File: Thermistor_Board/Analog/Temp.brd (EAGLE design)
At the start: 70 x 70 mm, 39 parts, among them J1 IO, J2 SJ-3523-SMT-TR, J3 SJ-3523-SMT-TR, J5 SJ-3523-SMT-TR

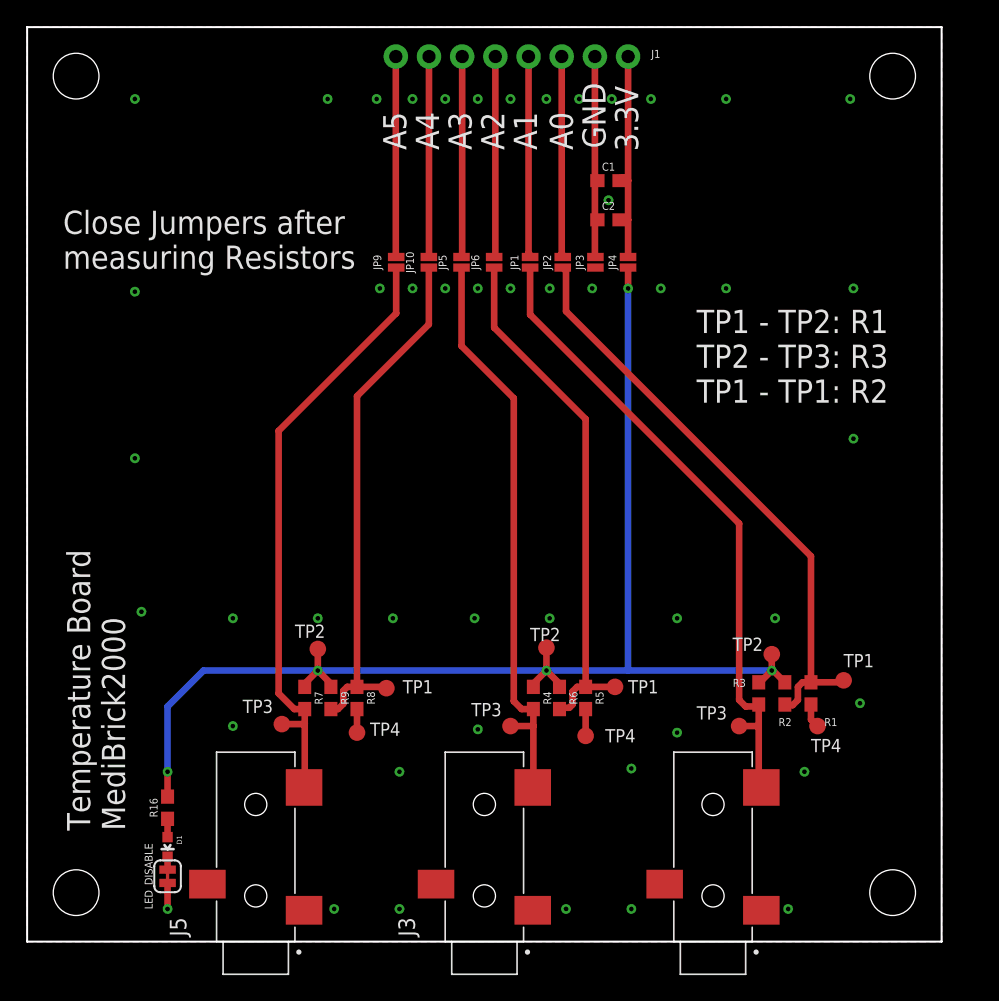
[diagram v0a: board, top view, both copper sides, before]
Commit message: Board Updates
All LEDs at same location
Separated analog and digital ground
Updated impedance components
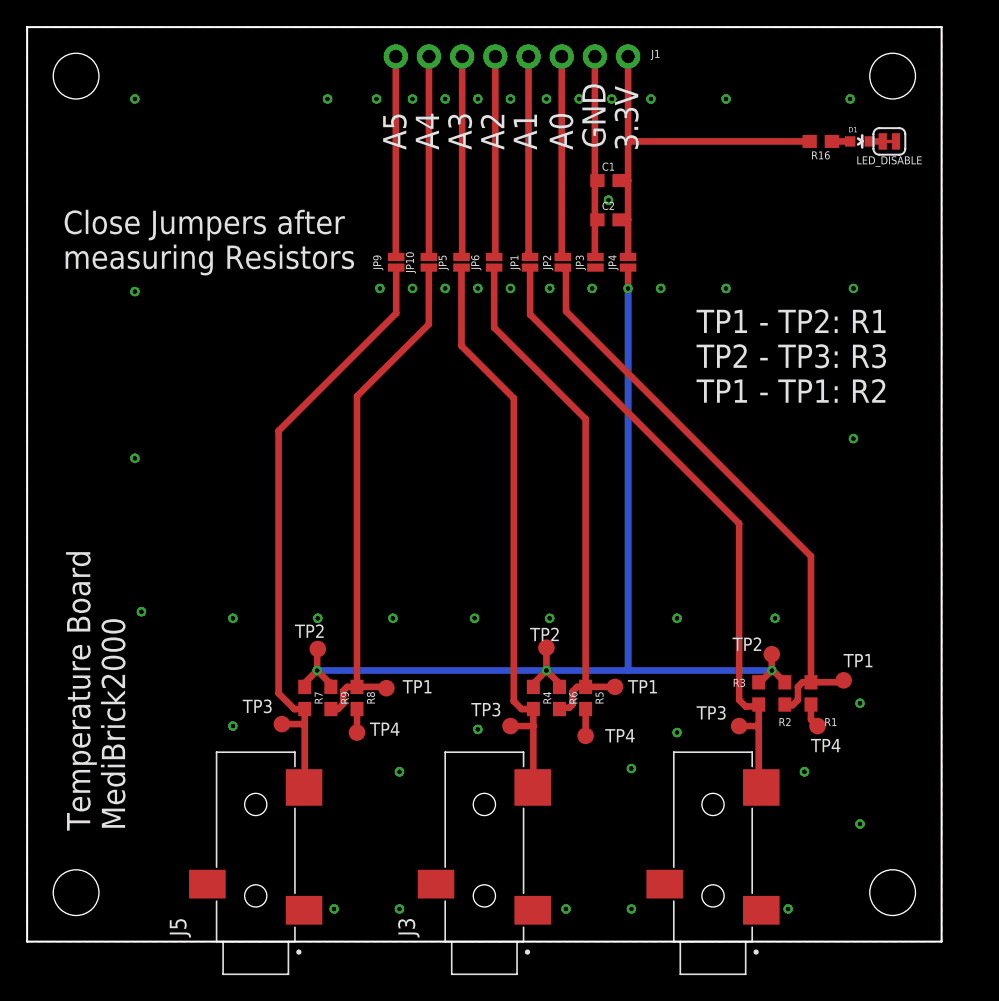
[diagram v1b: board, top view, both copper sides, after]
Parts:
- moved LED_DISABLE 78.8 mm to (66.0, 61.2), turned to 180 degrees
- moved D1 75.7 mm to (63.8, 61.2), turned to 270 degrees
- moved R16 71.4 mm to (60.8, 61.2), turned to 180 degrees
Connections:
- removed net N$12: J1.5, JP6.2
- net 3.3V: no longer R16.2
- net N$15: now also R16.2
- net N$16: now also J1.5, JP6.2
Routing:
- net 3.3V: track 99.7 -> 80.3 mm, vias 5 -> 4
- net N$16: track 16.0 -> 31.3 mm
- net N$12: track 15.4 -> 0.00 mm
- net N$15: track 17.2 -> 31.1 mm
- net GND: track 7.70 -> 5.71 mm
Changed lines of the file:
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@@
 <attribute name="VALUE" x="44.5" y="54.488" size="0.6096" layer="27" font="vector" ratio="20" align="top-center"/>
 </element>
-<element name="R16" library="SparkFun-Resistors" library_urn="urn:adsk.eagle:library:532" package="0603" package3d_urn="urn:adsk.eagle:package:39650/1" value="1k" x="10.75" y="10.25" smashed="yes" rot="R90">
-<attribute name="NAME" x="9.988" y="10.25" size="0.6096" layer="25" font="vector" ratio="20" rot="R90" align="bottom-center"/>
-<attribute name="PROD_ID" value="RES-07856" x="10.75" y="10.25" size="1.778" layer="27" rot="R90" display="off"/>
-<attribute name="VALUE" x="11.512" y="10.25" size="0.6096" layer="27" font="vector" ratio="20" rot="R90" align="top-center"/>
-</element>
-<element name="D1" library="SparkFun-LED" package="LED-0603" value="RED" x="10.75" y="7.25" smashed="yes" rot="R180">
-<attribute name="NAME" x="11.4485" y="8.139" size="0.4064" layer="25" rot="R270"/>
-<attribute name="PROD_ID" value="DIO-00819" x="13.75" y="0.25" size="1.778" layer="27" rot="R180" display="off"/>
-<attribute name="VALUE" x="9.6705" y="8.266" size="0.4064" layer="27" rot="R270"/>
-</element>
-<element name="LED_DISABLE" library="SparkFun-Jumpers" library_urn="urn:adsk.eagle:library:528" package="SMT-JUMPER_2_NC_TRACE_SILK" package3d_urn="urn:adsk.eagle:package:39281/1" value="JUMPER-SMT_2_NC_TRACE_SILK" x="10.75" y="5" smashed="yes" rot="R90">
-<attribute name="NAME" x="9.607" y="5" size="0.6096" layer="25" font="vector" ratio="20" rot="R90" align="bottom-center"/>
-<attribute name="VALUE" x="11.893" y="5" size="0.6096" layer="27" font="vector" ratio="20" rot="R90" align="top-center"/>
+<element name="R16" library="SparkFun-Resistors" library_urn="urn:adsk.eagle:library:532" package="0603" package3d_urn="urn:adsk.eagle:package:39650/1" value="1k" x="60.75" y="61.25" smashed="yes" rot="R180">
+<attribute name="NAME" x="60.75" y="60.488" size="0.6096" layer="25" font="vector" ratio="20" rot="R180" align="bottom-center"/>
+<attribute name="PROD_ID" value="RES-07856" x="60.75" y="61.25" size="1.778" layer="27" rot="R180" display="off"/>
+<attribute name="VALUE" x="60.75" y="62.012" size="0.6096" layer="27" font="vector" ratio="20" rot="R180" align="top-center"/>
+</element>
+<element name="D1" library="SparkFun-LED" package="LED-0603" value="RED" x="63.75" y="61.25" smashed="yes" rot="R270">
+<attribute name="NAME" x="62.861" y="61.9485" size="0.4064" layer="25"/>
+<attribute name="PROD_ID" value="DIO-00819" x="70.75" y="64.25" size="1.778" layer="27" rot="R270" display="off"/>
+<attribute name="VALUE" x="62.734" y="60.1705" size="0.4064" layer="27"/>
+</element>
+<element name="LED_DISABLE" library="SparkFun-Jumpers" library_urn="urn:adsk.eagle:library:528" package="SMT-JUMPER_2_NC_TRACE_SILK" package3d_urn="urn:adsk.eagle:package:39281/1" value="JUMPER-SMT_2_NC_TRACE_SILK" x="66" y="61.25" smashed="yes" rot="R180">
+<attribute name="NAME" x="66" y="60.107" size="0.6096" layer="25" font="vector" ratio="20" rot="R180" align="bottom-center"/>
+<attribute name="VALUE" x="66" y="62.393" size="0.6096" layer="27" font="vector" ratio="20" rot="R180" align="top-center"/>
 </element>
 <element name="FRAME1" library="SparkFun-Aesthetics" library_urn="urn:adsk.eagle:library:507" package="DUMMY" package3d_urn="urn:adsk.eagle:package:37104/1" value="FRAME-LETTERNO_PACKAGE" x="-0.25" y="-5.25" smashed="yes">
@@
 <signals>
 <signal name="3.3V">
-<contactref element="R16" pad="2"/>
-<via x="10.75" y="13" extent="1-16" drill="0.35"/>
-<wire x1="10.75" y1="11.1" x2="10.75" y2="13" width="0.508" layer="1"/>
 <via x="57" y="20.75" extent="1-16" drill="0.35"/>
-<wire x1="13.5" y1="20.75" x2="10.75" y2="18" width="0.508" layer="16"/>
-<wire x1="10.75" y1="18" x2="10.75" y2="13" width="0.508" layer="16"/>
 <wire x1="57" y1="20.75" x2="46" y2="20.75" width="0.508" layer="16"/>
 <wire x1="46" y1="20.75" x2="39.75" y2="20.75" width="0.508" layer="16"/>
@@
 <contactref element="JP4" pad="1"/>
 <contactref element="TP1" pad="P$1"/>
-<wire x1="39.75" y1="20.75" x2="22.25" y2="20.75" width="0.508" layer="16"/>
-<wire x1="22.25" y1="20.75" x2="13.5" y2="20.75" width="0.508" layer="16"/>
+<wire x1="39.75" y1="20.75" x2="22.2" y2="20.75" width="0.508" layer="16"/>
 <wire x1="57" y1="22" x2="57" y2="21.5" width="0.508" layer="1"/>
 <contactref element="R9" pad="1"/>
@@
 <wire x1="57" y1="20.75" x2="57.1" y2="20.75" width="0.508" layer="1"/>
 <wire x1="57.1" y1="20.75" x2="58" y2="19.85" width="0.508" layer="1"/>
-<via x="22.25" y="20.75" extent="1-16" drill="0.35"/>
-<wire x1="21.25" y1="19.5" x2="21.25" y2="19.75" width="0.508" layer="1"/>
-<wire x1="21.25" y1="19.75" x2="22.25" y2="20.75" width="0.508" layer="1"/>
-<wire x1="22.25" y1="20.75" x2="23.25" y2="19.75" width="0.508" layer="1"/>
-<wire x1="23.25" y1="19.75" x2="23.25" y2="19.5" width="0.508" layer="1"/>
-<wire x1="22.25" y1="20.75" x2="22.25" y2="22.4" width="0.508" layer="1"/>
+<via x="22.2" y="20.75" extent="1-16" drill="0.35"/>
+<wire x1="21.25" y1="19.5" x2="21.25" y2="19.8" width="0.508" layer="1"/>
+<wire x1="21.25" y1="19.8" x2="22.2" y2="20.75" width="0.508" layer="1"/>
+<wire x1="23.25" y1="19.809809375" x2="23.146109375" y2="19.803890625" width="0.508" layer="1"/>
+<wire x1="22.2" y1="20.75" x2="23.146109375" y2="19.803890625" width="0.508" layer="1"/>
+<wire x1="23.25" y1="19.809809375" x2="23.25" y2="19.5" width="0.508" layer="1"/>
+<wire x1="22.25" y1="22.4" x2="22.2" y2="22.35" width="0.508" layer="1"/>
+<wire x1="22.2" y1="22.35" x2="22.2" y2="20.75" width="0.508" layer="1"/>
 <via x="46" y="50" extent="1-16" drill="0.35"/>
 <wire x1="46" y1="50" x2="46" y2="20.75" width="0.508" layer="16"/>
@@
 <via x="8.25" y="64.5" extent="1-16" drill="0.35"/>
 <contactref element="LED_DISABLE" pad="1"/>
-<wire x1="10.75" y1="4.492" x2="10.75" y2="2.5" width="0.508" layer="1"/>
-<via x="10.75" y="2.5" extent="1-16" drill="0.35"/>
+<via x="63.75" y="9" extent="1-16" drill="0.35"/>
 <polygon width="0.508" layer="16" isolate="0.254">
 <vertex x="0" y="70"/>
@@
 <contactref element="R16" pad="1"/>
 <contactref element="D1" pad="A"/>
-<wire x1="10.75" y1="9.4" x2="10.75" y2="8" width="0.508" layer="1"/>
+<wire x1="61.6" y1="61.25" x2="63" y2="61.25" width="0.508" layer="1"/>
 </signal>
 <signal name="N$28">
 <contactref element="D1" pad="C"/>
 <contactref element="LED_DISABLE" pad="2"/>
-<wire x1="10.75" y1="5.508" x2="10.75" y2="6.5" width="0.508" layer="1"/>
+<wire x1="65.492" y1="61.25" x2="64.5" y2="61.25" width="0.508" layer="1"/>
 </signal>
 <signal name="N$1">
@@
 <wire x1="30.76" y1="52.4164" x2="30.75" y2="52.4064" width="0.508" layer="1"/>
 </signal>
-<signal name="N$12">
-<contactref element="J1" pad="5"/>
-<contactref element="JP6" pad="2"/>
-<wire x1="35.84" y1="67.75" x2="35.84" y2="52.4964" width="0.508" layer="1"/>
-<wire x1="35.84" y1="52.4964" x2="35.75" y2="52.4064" width="0.508" layer="1"/>
-</signal>
 <signal name="N$10">
 <contactref element="JP9" pad="2"/>
@@
 <wire x1="45.875" y1="58.375" x2="45.75" y2="58.5" width="0.508" layer="1"/>
 <wire x1="45.75" y1="58.5" x2="45.5" y2="58.5" width="0.508" layer="1"/>
-<wire x1="46" y1="67.75" x2="46" y2="58.25" width="0.508" layer="1"/>
+<wire x1="46" y1="67.75" x2="46" y2="61.25" width="0.508" layer="1"/>
+<wire x1="46" y1="61.25" x2="46" y2="58.25" width="0.508" layer="1"/>
 <wire x1="45.35" y1="58.25" x2="45.475" y2="58.375" width="0.508" layer="1"/>
 <wire x1="45.475" y1="58.375" x2="45.875" y2="58.375" width="0.508" layer="1"/>
+<contactref element="R16" pad="2"/>
+<wire x1="59.9" y1="61.25" x2="46" y2="61.25" width="0.508" layer="1"/>
 </signal>
 <signal name="N$16">
@@
 <wire x1="43.5" y1="52.4064" x2="43.46" y2="52.4464" width="0.508" layer="1"/>
 <wire x1="43.46" y1="52.4464" x2="43.46" y2="52.6115" width="0.508" layer="1"/>
+<contactref element="J1" pad="5"/>
+<contactref element="JP6" pad="2"/>
+<wire x1="35.84" y1="67.75" x2="35.84" y2="52.4964" width="0.508" layer="1"/>
+<wire x1="35.84" y1="52.4964" x2="35.75" y2="52.4064" width="0.508" layer="1"/>
+<wire x1="35.84" y1="67.75" x2="43.46" y2="67.75" width="0" layer="19" extent="1-1"/>
 </signal>
 </signals>

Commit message: Board Updates
Separated analog and digital ground
Updated routing
Updated silk labeling
Sound board with ES8388 included
Impedance and ECG board
Working on IMU board
Working on Environmental Airquality board
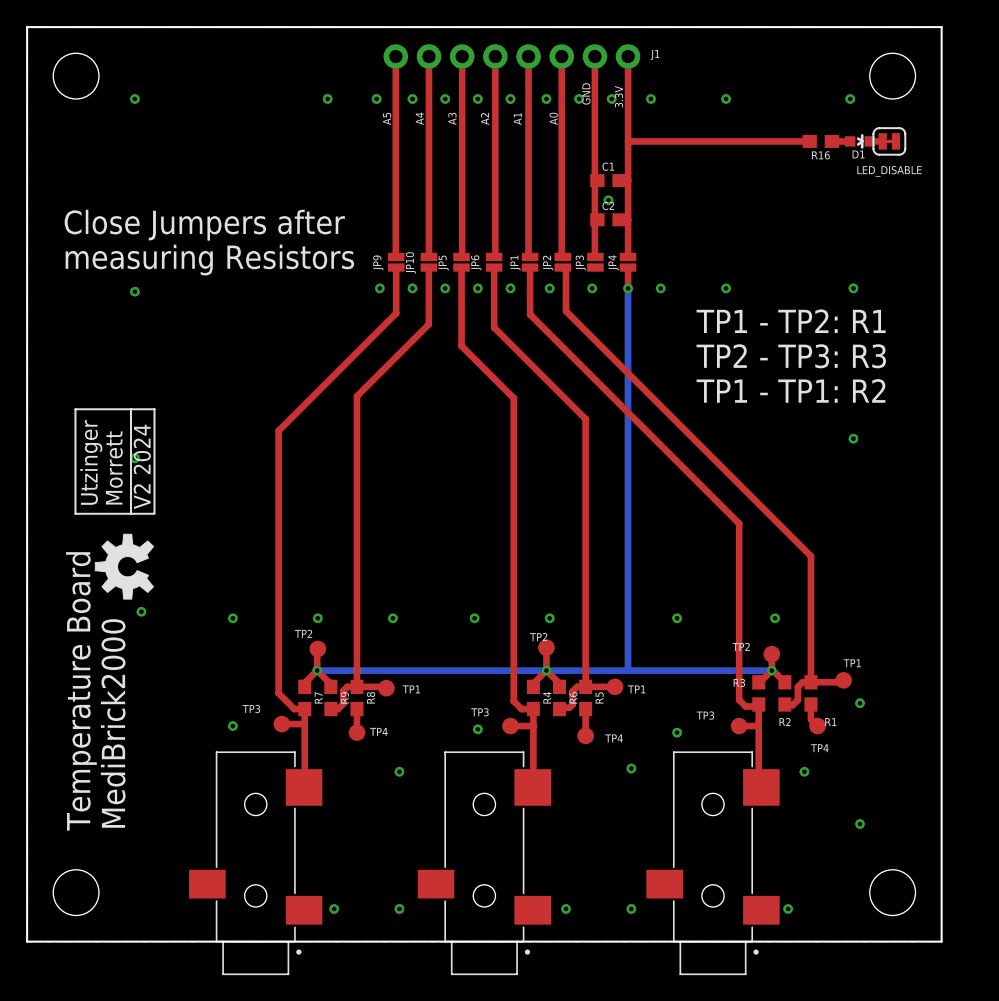
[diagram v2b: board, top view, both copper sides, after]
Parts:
- added U$1: (no value), SparkFun-Aesthetics:OSHW-LOGO-M
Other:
- board text added: "Utzinger Morrett"
- board text added: "V2 2024"
